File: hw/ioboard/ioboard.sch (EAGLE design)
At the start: 33 parts, among them IC1 MAX232, M1 ENC_MODULE, X2 2540-

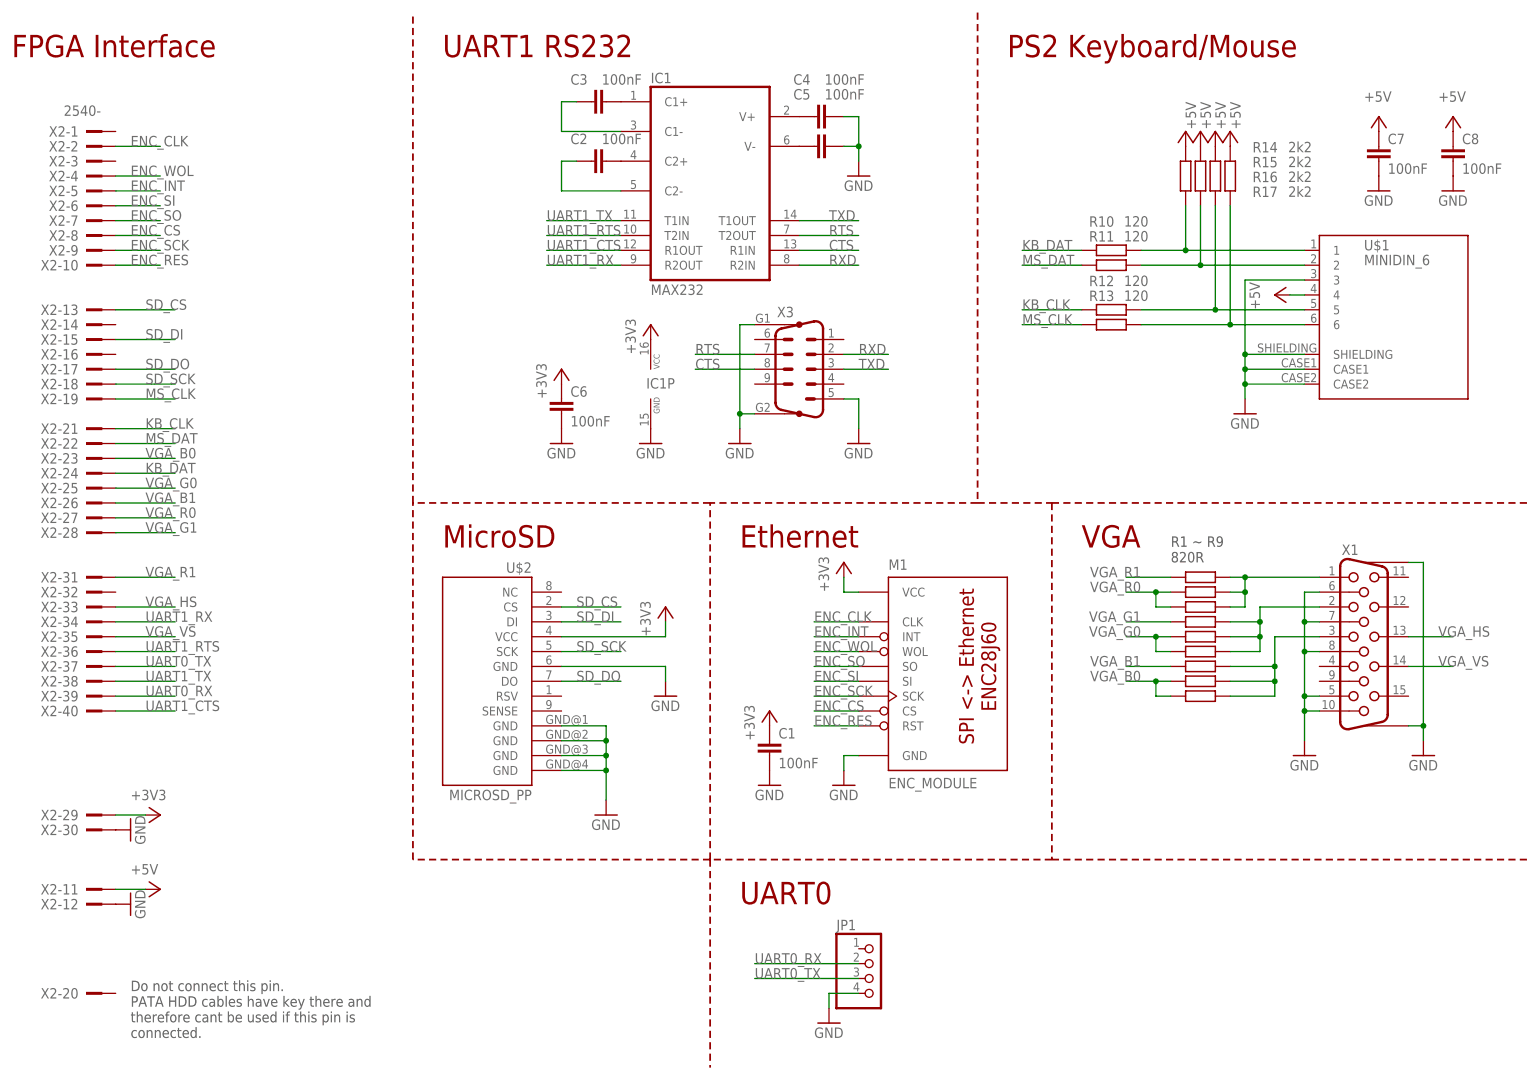
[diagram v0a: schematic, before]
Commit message: New version of IO board - fix issue #2 but remove SD card and ethernet ... not need at this time anyway
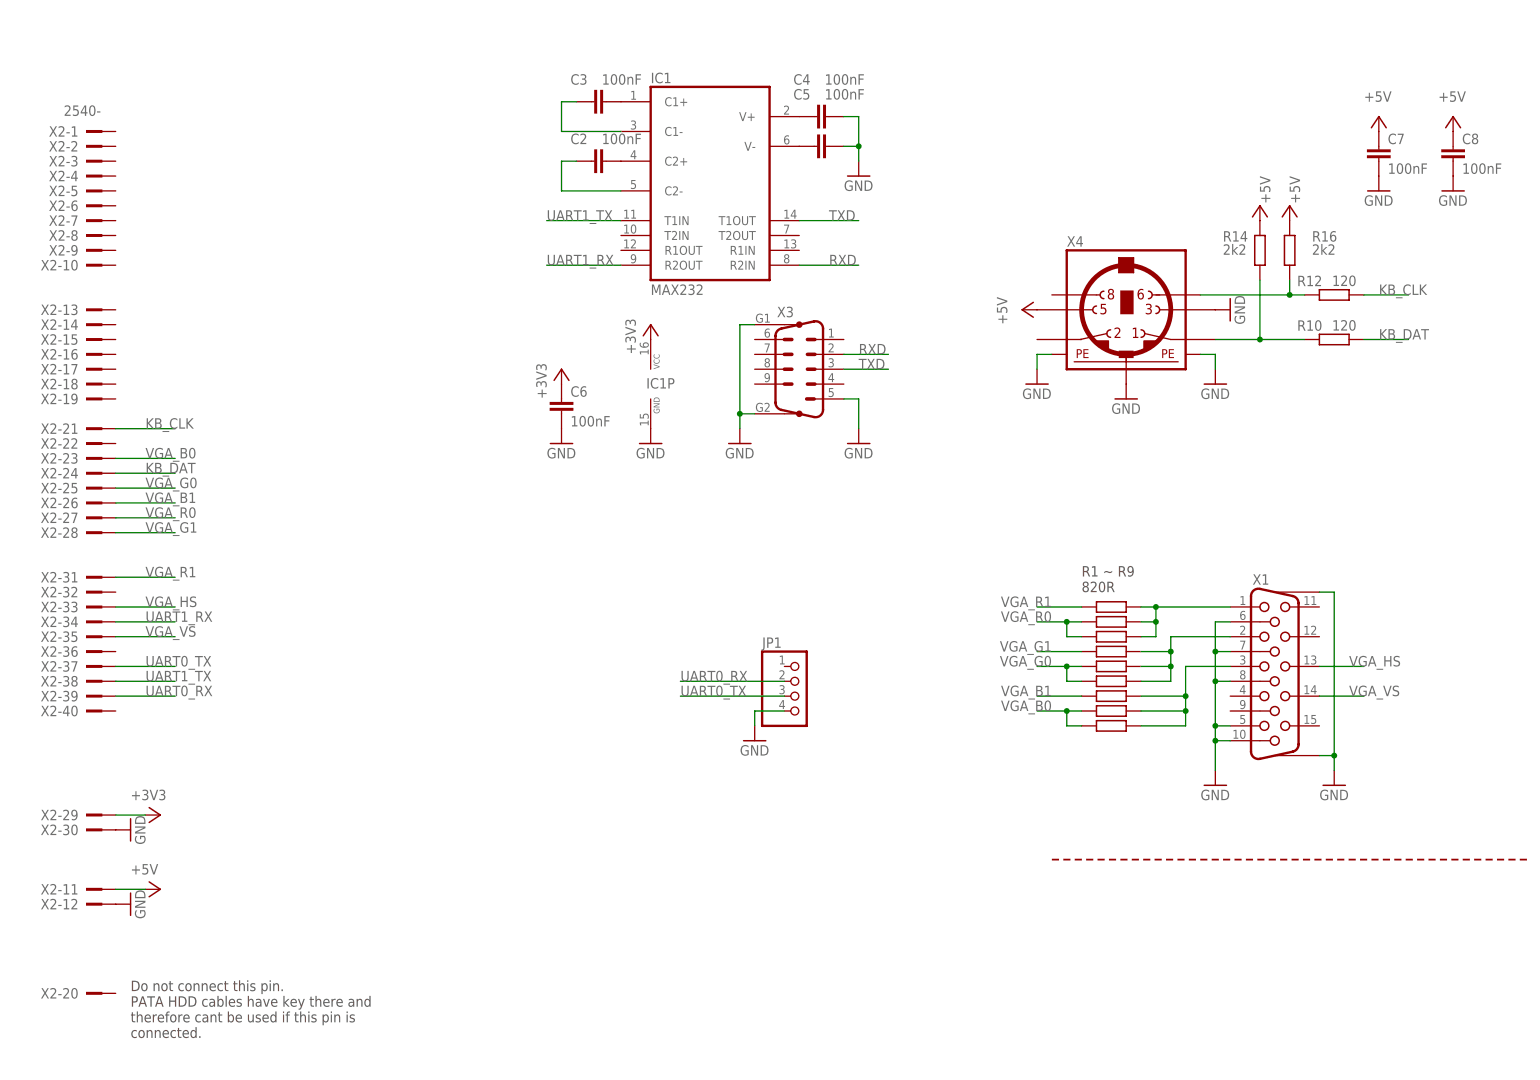
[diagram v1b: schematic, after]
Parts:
- removed C1: 100nF, rcl:C-EU025-025X050
- removed M1: ENC_MODULE, VladisLib:ENC_MODULE
- removed R11, R13: 120, rcl:R-EU_0204/7
- removed R15, R17: 2k2, rcl:R-EU_0204/7
- removed U$1: MINIDIN_6, VladisLib:MINIDIN_6
- removed U$2: MICROSD_PP, DE1594-v2:MICROSD_PP
- added X4: (no value), mini_din:MINI_DIN_6
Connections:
- removed net CTS: IC1G$1.R1IN, X3.8
- removed net ENC_CLK: M1.CLK, X2-2.KL
- removed net ENC_CS: M1.CS, X2-8.KL
- removed net ENC_INT: M1.INT, X2-5.KL
- removed net ENC_RES: M1.RST, X2-10.KL
- removed net ENC_SCK: M1.SCK, X2-9.KL
- removed net ENC_SI: M1.SI, X2-6.KL
- removed net ENC_SO: M1.SO, X2-7.KL
- removed net ENC_WOL: M1.WOL, X2-4.KL
- removed net MS_CLK: R13.1, X2-19.KL
- removed net MS_DAT: R11.1, X2-22.KL
- removed net N$3: R12.2, R16.1, U$1.5
- removed net N$4: R13.2, R17.1, U$1.6
- removed net RTS: IC1G$1.T2OUT, X3.7
- removed net SD_CS: U$2.CS, X2-13.KL
- removed net SD_DI: U$2.DI, X2-15.KL
- removed net SD_DO: U$2.DO, X2-17.KL
- removed net SD_SCK: U$2.SCK, X2-18.KL
- removed net UART1_CTS: IC1G$1.R1OUT, X2-40.KL
- removed net UART1_RTS: IC1G$1.T2IN, X2-36.KL
- net +3V3: no longer C1.1, M1.VCC, U$2.VCC
- net +5V: now also X4.5; no longer R15.2, R17.2, U$1.4
- net GND: now also X4.3, X4.PE1, X4.PE2, X4.PE3; no longer C1.2, M1.GND, U$1.3, U$1.CASE1, U$1.CASE2, U$1.SHIELDING, U$2.GND, U$2.GND@1, U$2.GND@2, U$2.GND@3, U$2.GND@4
- net N$1: now also R12.2, R16.1, X4.6; no longer R10.2, R14.1, U$1.1
- net N$2: now also R10.2, R14.1, X4.1; no longer R11.2, R15.1, U$1.2
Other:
- note removed: "Ethernet"
- note removed: "FPGA Interface"
- note removed: "MicroSD"
- note removed: "PS2 Keyboard/Mouse"
- note removed: "UART0"
- note removed: "UART1 RS232"
- note removed: "VGA"
- moved on the sheet: JP1, R10, R12, R14, R16, X1
